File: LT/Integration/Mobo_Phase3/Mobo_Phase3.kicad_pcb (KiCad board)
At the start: 4 copper layers, 90.2 x 95.9 mm, 112 parts, among them J1 Bus, J10 Conn_01x02_Female, J11 Conn_01x02_Male, J12 Conn_01x02_Male, J13 Conn_01x02_Male, J14 Conn_01x02_Female, J15 Conn_Coaxial, J2 Conn_Coaxial, J3 Conn_Coaxial, J4 Conn_Coaxial, J6 Conn_Coaxial, J7 Conn_Coaxial, J8 Conn_Coaxial, J9 Conn_Coaxial, Q1 2N5486, Q2 Q_NJFET_DSG, Q3 Q_NPN_BEC, Q4 Q_PNP_BEC, T1 Transformer_1P_SS, T2 Transformer_1P_SS, U1 BAP64Q

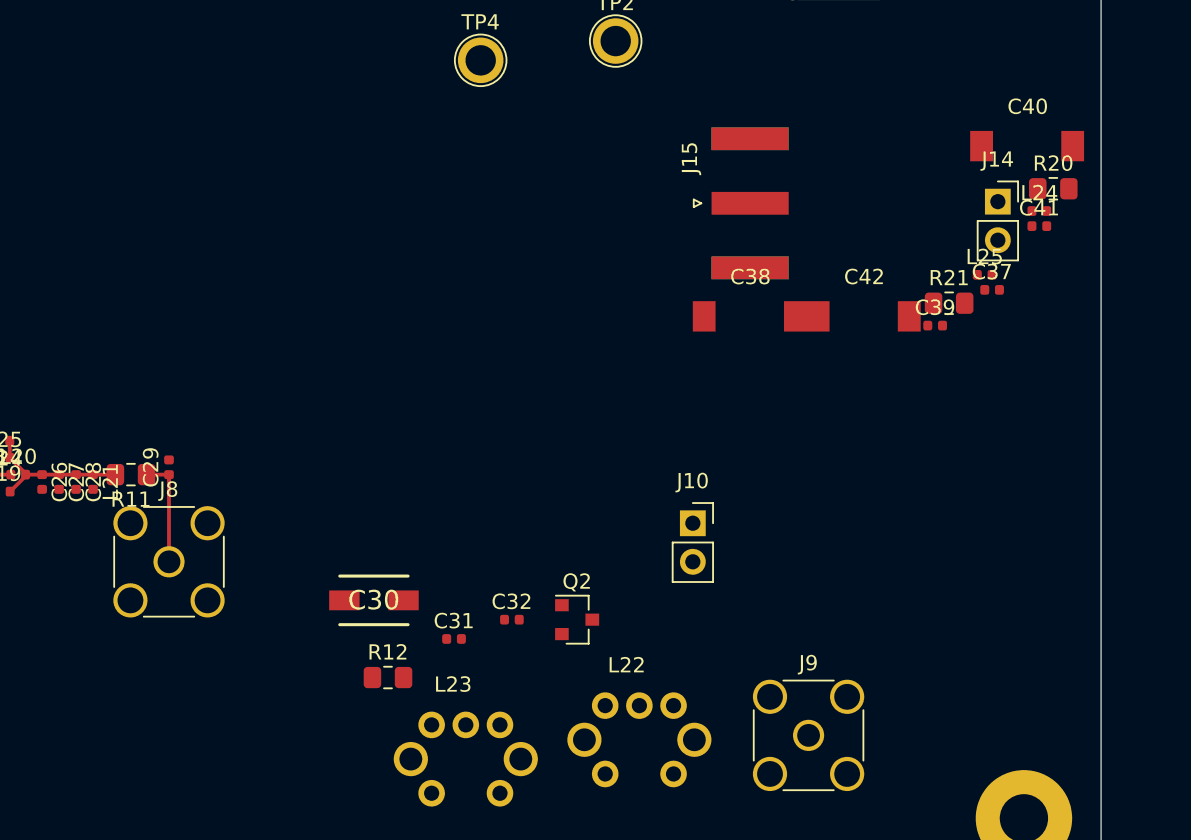
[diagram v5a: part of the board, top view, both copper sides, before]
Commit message: Finished 29.4 MHz LPF PCB layout for Phase 3 of Transmitting Stage. 2/4 Complete
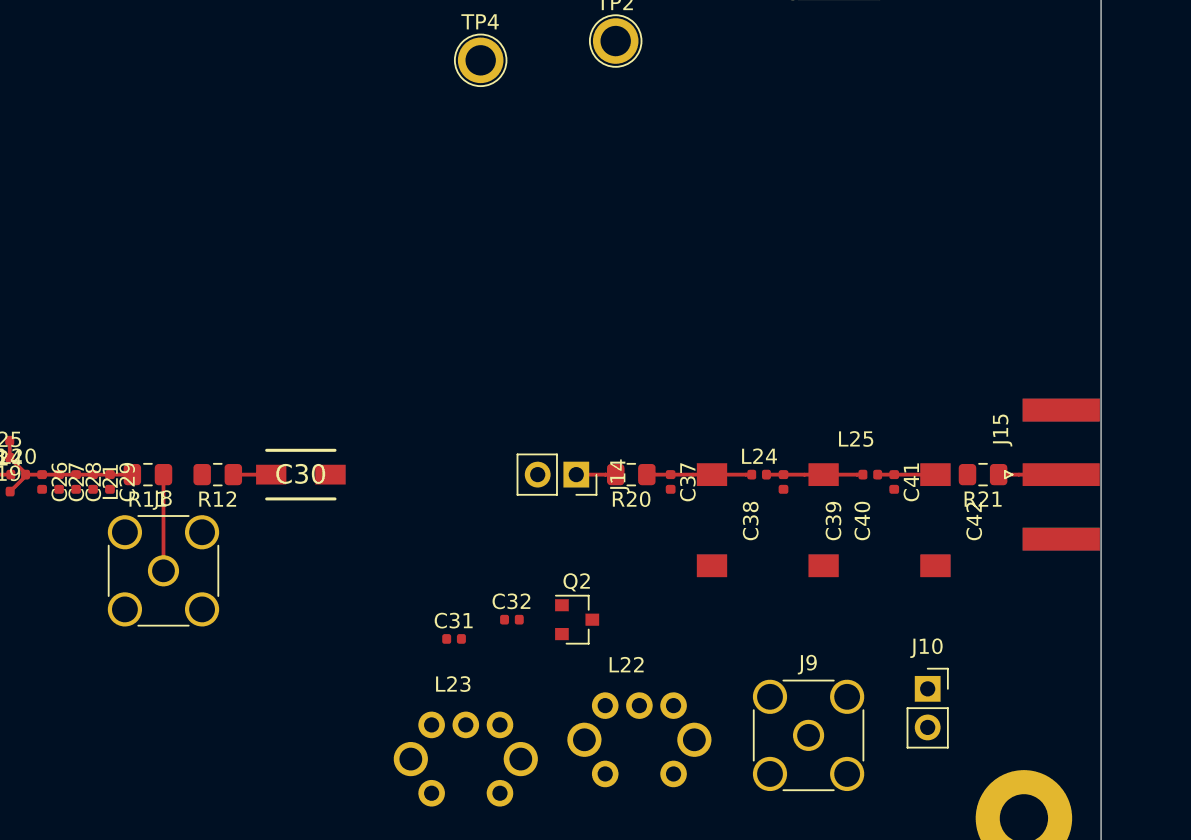
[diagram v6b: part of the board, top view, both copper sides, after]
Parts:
- moved R20 33.6 mm to (187.7, 104.7), turned to 180 degrees
- moved J14 33.1 mm to (184.1, 104.7), turned to 270 degrees
- moved J15 27.2 mm to (216.0, 104.7)
- moved L24 25.3 mm to (196.1, 104.7)
- moved C37 24.7 mm to (190.3, 105.2), turned to 270 degrees
- moved C40 24.0 mm to (200.4, 104.7), turned to 270 degrees
- moved C41 19.4 mm to (205.0, 105.2), turned to 270 degrees
- moved J10 18.9 mm to (207.2, 118.9)
- moved R12 17.4 mm to (160.5, 104.7), turned to 180 degrees
- moved L25 15.2 mm to (203.5, 104.7)
- moved C39 14.3 mm to (197.7, 105.2), turned to 270 degrees
- moved C42 13.0 mm to (207.7, 104.7), turned to 270 degrees
- moved R21 11.5 mm to (210.9, 104.7), turned to 180 degrees
- moved C38 10.4 mm to (193.0, 104.7), turned to 270 degrees
- moved C30 9.58 mm to (166.0, 104.7), turned to 180 degrees
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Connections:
- C29 pad 1: /29.4 MHz Bandpass Filter/29.4BPF_OUT -> Net-(C24-Pad1)
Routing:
- net Net-(C37-Pad1): track 0.00 -> 6.90 mm
- net Net-(C39-Pad1): track 0.00 -> 6.35 mm
- net Net-(J15-Pad1): track 0.00 -> 4.12 mm
- net Net-(C41-Pad1): track 0.00 -> 3.81 mm
- net /Low Pass Filter/PA_OUT: track 0.00 -> 2.61 mm
- net Net-(C30-Pad2): track 0.00 -> 2.50 mm
- net Net-(C24-Pad1): track 10.1 -> 11.2 mm
- net /29.4 MHz Bandpass Filter/29.4BPF_OUT: track 7.22 -> 6.33 mm

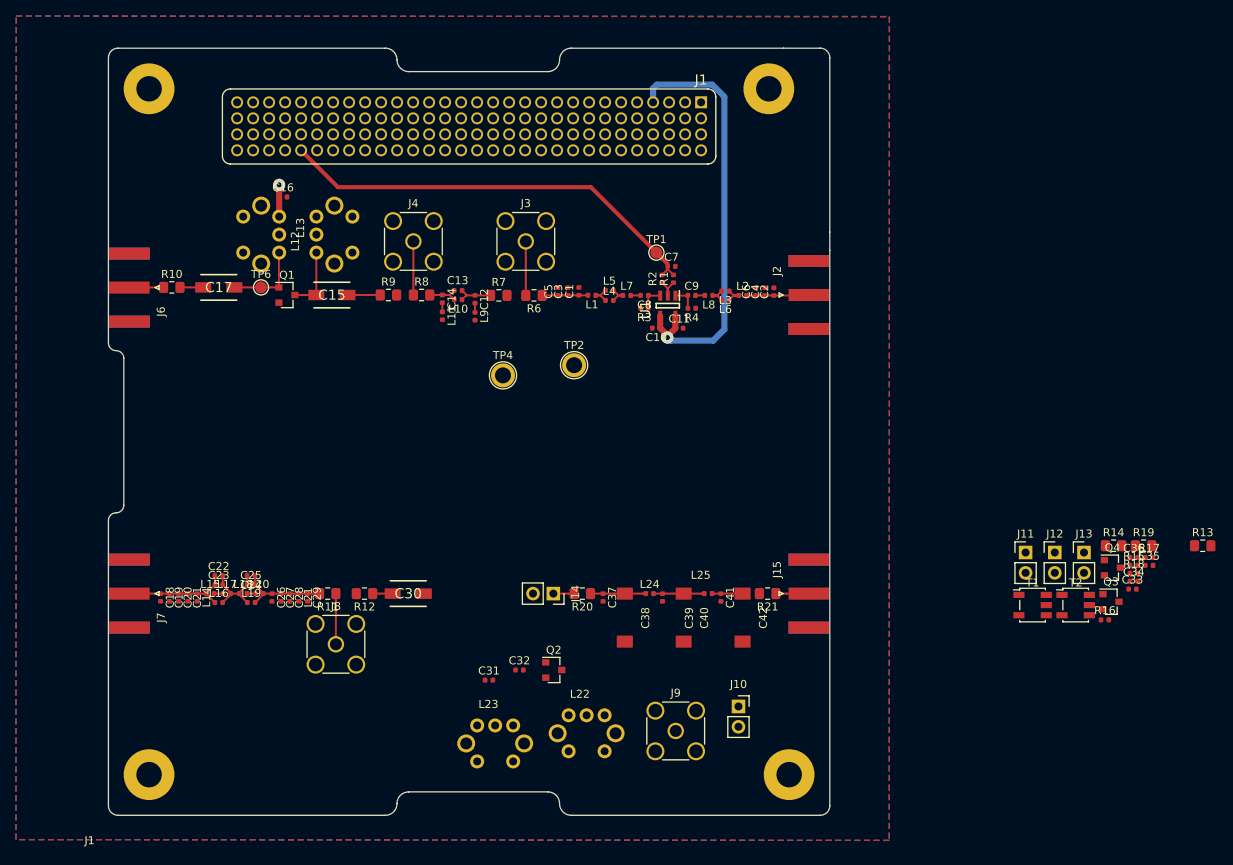
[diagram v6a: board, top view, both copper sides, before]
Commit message: Finished Pre-Amplifier PCB layout for Transmitting Stage. 3/4 Complete
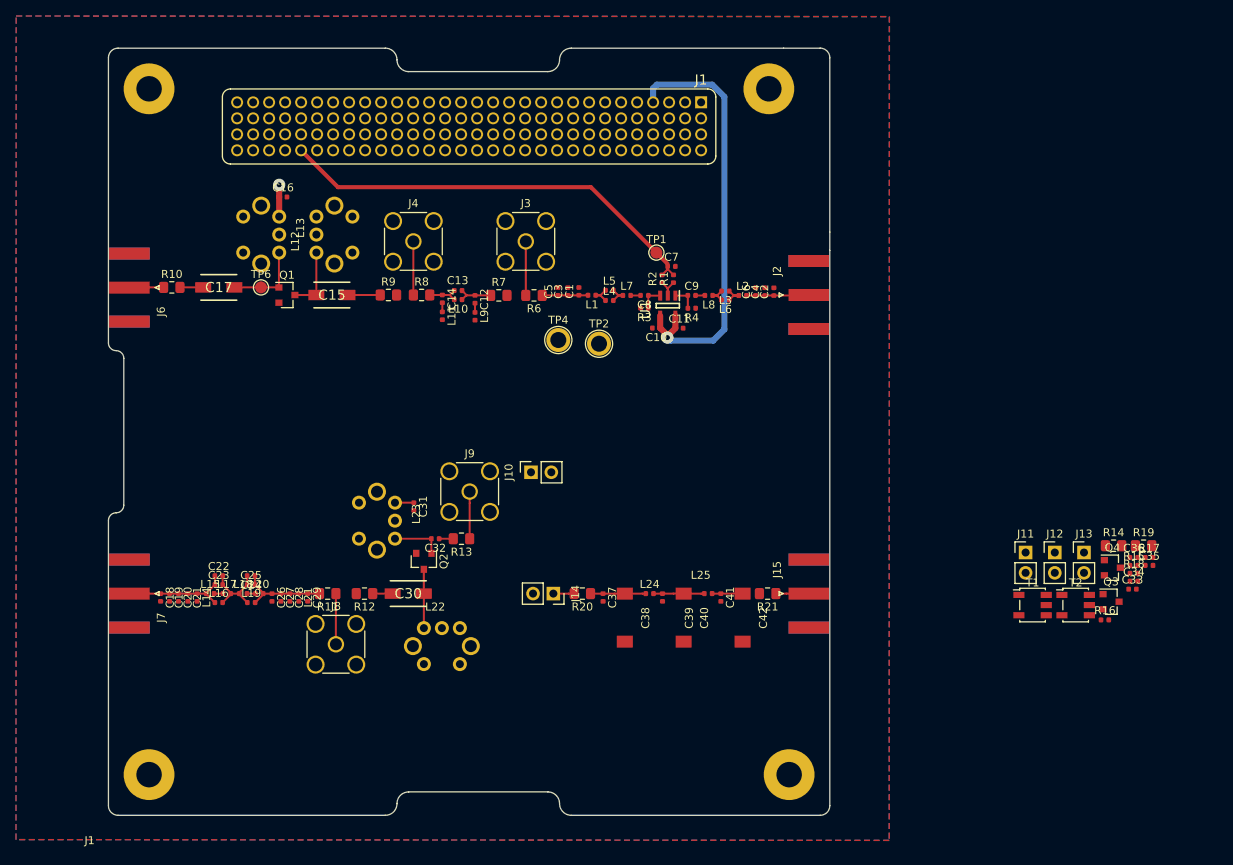
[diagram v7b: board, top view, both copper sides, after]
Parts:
- moved R13 92.7 mm to (172.6, 97.9), turned to 180 degrees
- moved J9 39.5 mm to (173.6, 92.0)
- moved J10 39.1 mm to (181.3, 89.6), turned to 90 degrees
- moved L23 31.5 mm to (162.0, 95.6), turned to 270 degrees
- moved C31 23.6 mm to (166.7, 93.9), turned to 270 degrees
- moved Q2 21.2 mm to (167.9, 100.7), turned to 270 degrees
- moved L22 21.1 mm to (170.2, 111.3)
- moved C32 19.5 mm to (169.3, 97.9), turned to 180 degrees
- moved TP4 8.21 mm to (184.7, 73.1)
- moved TP2 4.11 mm to (189.8, 73.5)
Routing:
- net Net-(C30-Pad1): track 0.00 -> 7.36 mm
- net Net-(C32-Pad2): track 0.00 -> 6.38 mm
- net Net-(J10-Pad1): track 0.00 -> 5.89 mm
- net +8V: track 3.98 -> 6.33 mm
- net Net-(C32-Pad1): track 0.00 -> 1.77 mm

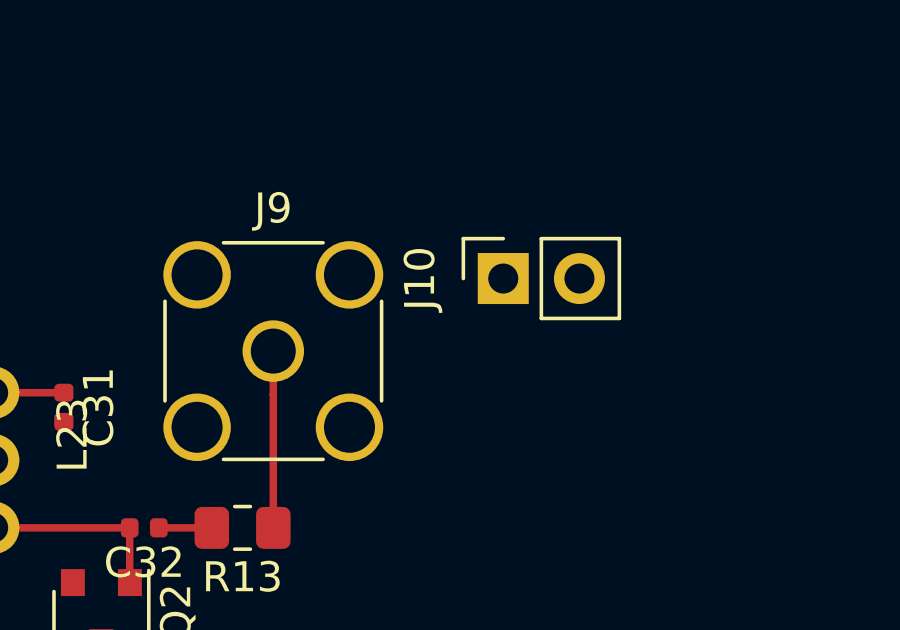
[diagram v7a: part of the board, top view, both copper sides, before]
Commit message: Fixed some minor layout issues on the motherboard
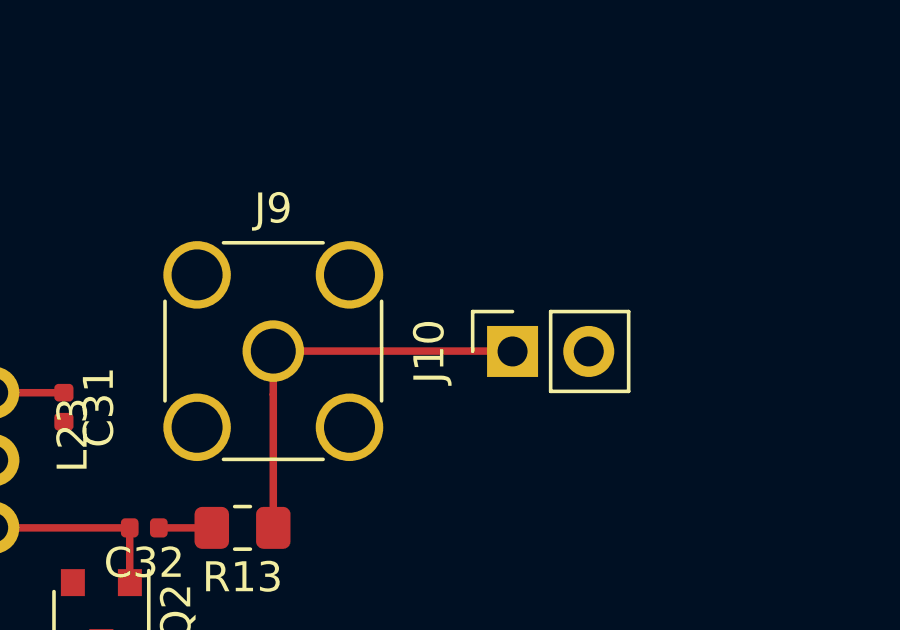
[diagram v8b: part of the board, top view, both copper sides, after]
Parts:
- moved J10 2.45 mm to (181.6, 92.0)
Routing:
- net Net-(J10-Pad1): track 5.89 -> 13.9 mm
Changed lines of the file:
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@@
     (thickness 1.6)
     (drawings 1)
-    (tracks 157)
+    (tracks 159)
     (zones 0)
     (modules 112)
@@
   )
   (module Connector_PinSocket_2.54mm:PinSocket_1x02_P2.54mm_Vertical (layer F.Cu)
-    (at 181.30012 89.58072 90)
+    (at 181.61 92.0115 90)
     (descr "Through hole straight socket strip, 1x02, 2.54mm pitch, single row (from Kicad 4.0.7), script generated")
     (tags "Through hole socket strip THT 1x02 2.54mm single row")
@@
   (segment (start 173.6344 93.448368) (end 173.6344 97.8916) (width 0.25) (layer F.Cu) (net 168))
   (segment (start 173.6344 91.9988) (end 173.6344 93.448368) (width 0.25) (layer F.Cu) (net 168))
+  (segment (start 181.5973 91.9988) (end 181.61 92.0115) (width 0.25) (layer F.Cu) (net 168))
+  (segment (start 173.6344 91.9988) (end 181.5973 91.9988) (width 0.25) (layer F.Cu) (net 168))
   (segment (start 195.25132 104.7496) (end 193.02984 104.7496) (width 0.25) (layer F.Cu) (net 173))
   (segment (start 195.64632 104.7496) (end 195.25132 104.7496) (width 0.25) (layer F.Cu) (net 173))
